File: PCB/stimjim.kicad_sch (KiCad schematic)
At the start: 21 parts, among them J1 Conn_02x08_Odd_Even, J10 USB4105-GF-A, J11 BM03B-SRSS-TB, J4 10129383-910002ALF, U151 AP2112K-3.3

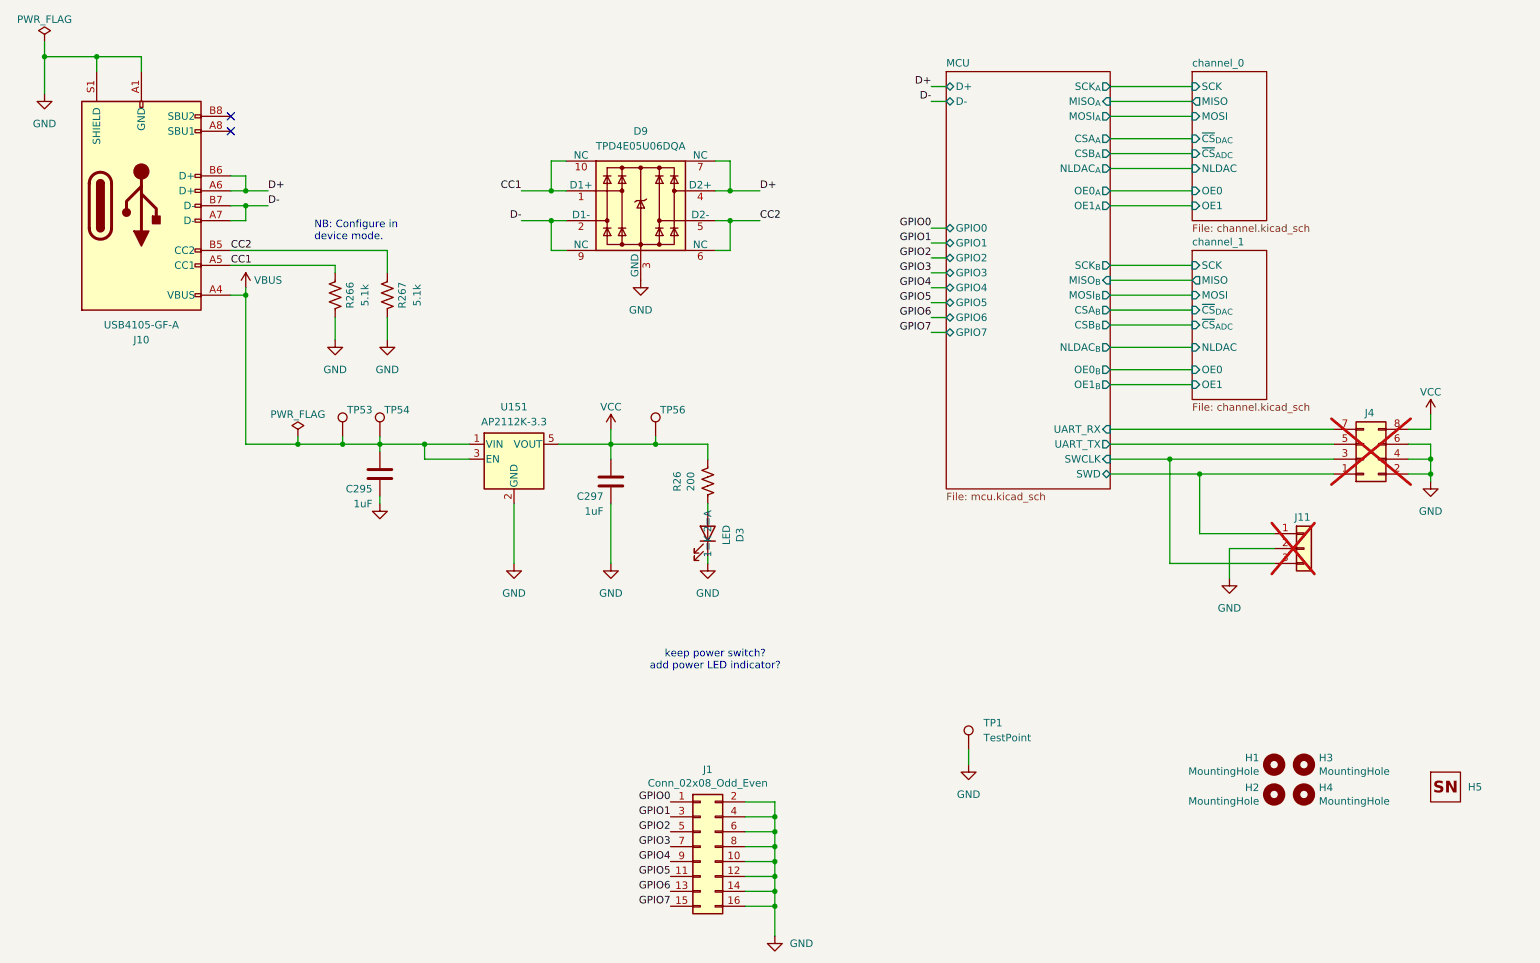
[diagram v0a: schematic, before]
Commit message: Stimjim Rev. B candidate
- Sent to fab
- Lots of manufacturability changes
- BOM consolidation
- Repo layout changed a bit to remove redundant information. e.g.
  datasheet links are embedded in schematic. BOM information embedded in
  schematic. etc
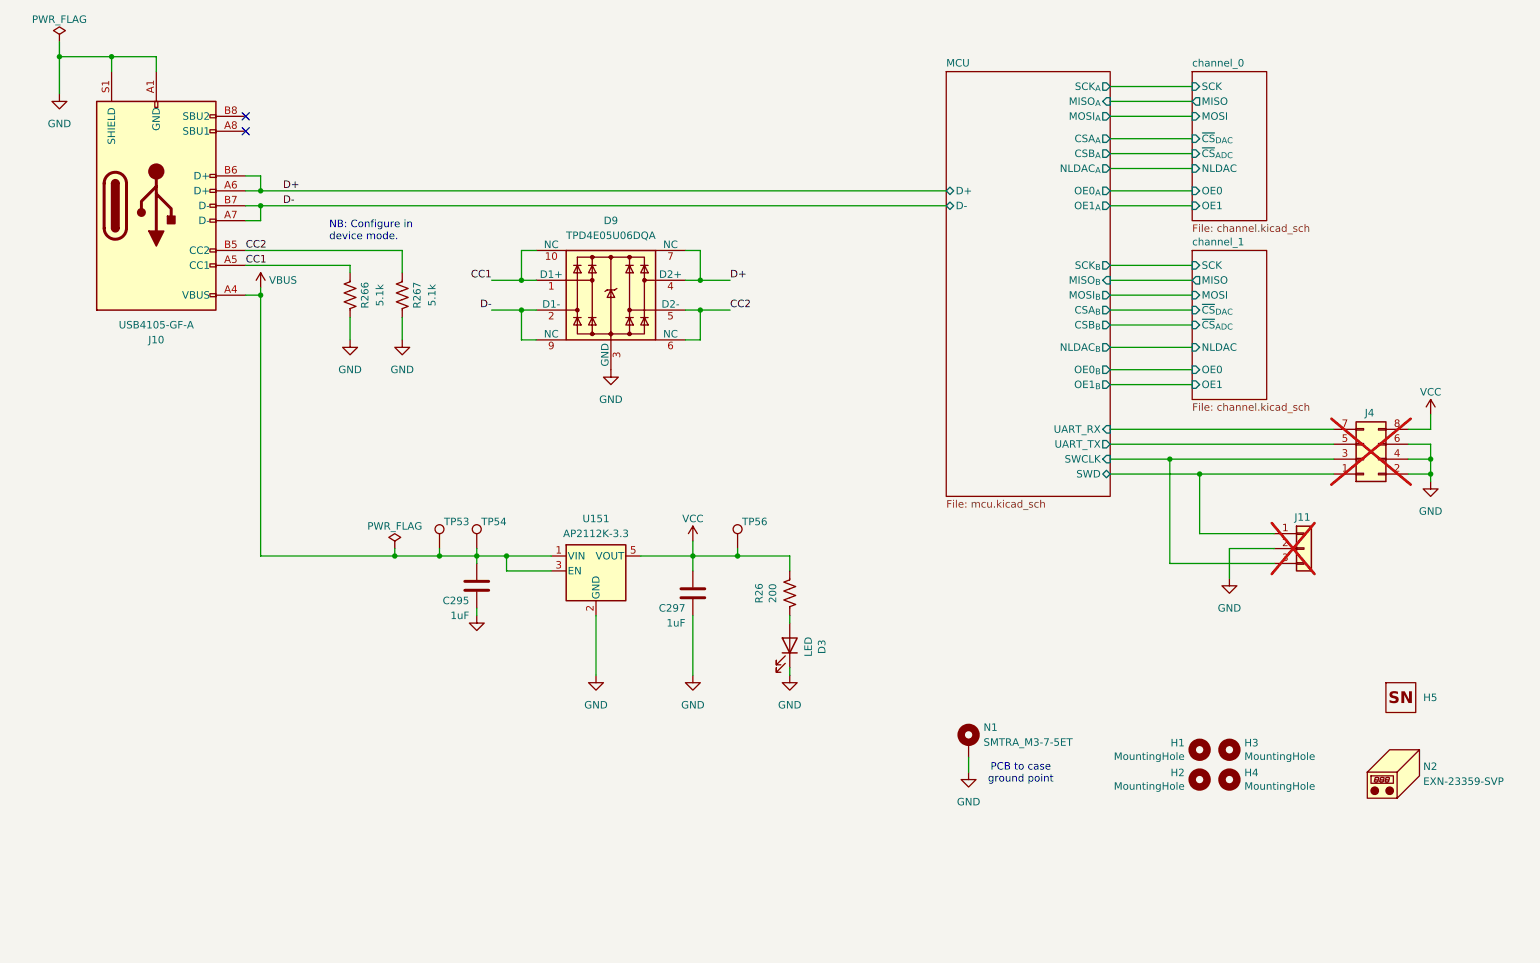
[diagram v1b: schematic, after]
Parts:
- removed J1: Conn_02x08_Odd_Even, Connector_IDC:IDC-Header_2x08_P2.54mm_Horizontal, symbol Connector_Generic:Conn_02x08_Odd_Even
- added N2: EXN-23359-SVP, symbol Mechanical:Housing
- C295, C297: Voltage 16V -> 25V
- D3: MPN (none) -> SSF-LXH100GD-01; now in the parts list
- D9: MPN (none) -> TPD4E05U06DQA
- J10: MPN (none) -> USB4105-GF-A
- J11: MPN (none) -> BM03B-SRSS-TB
- J4: MPN (none) -> 10129383-910002ALF
- N1: renamed from TP1; value TestPoint -> SMTRA_M3-7-5ET; symbol Connector:TestPoint -> Mechanical:MountingHole_Pad; MPN (none) -> SMTRA_M3-7-5ET
- R266, R267: Tolerance (none) -> 1%
- U151: MPN (none) -> AP2112K-3.3
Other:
- sheet MCU ports: added none; removed GPIO0, GPIO1, GPIO2, GPIO3, GPIO4, GPIO5, GPIO6, GPIO7
- note added: "PCB to case ground point"
- note removed: "keep power switch? add power LED indicator?"
- company: Nate Cermak and Jon Newman -> (none)
- moved on the sheet: C295, C297, D3, D9, H1, H2, H3, H4, H5, J10, R26, R266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

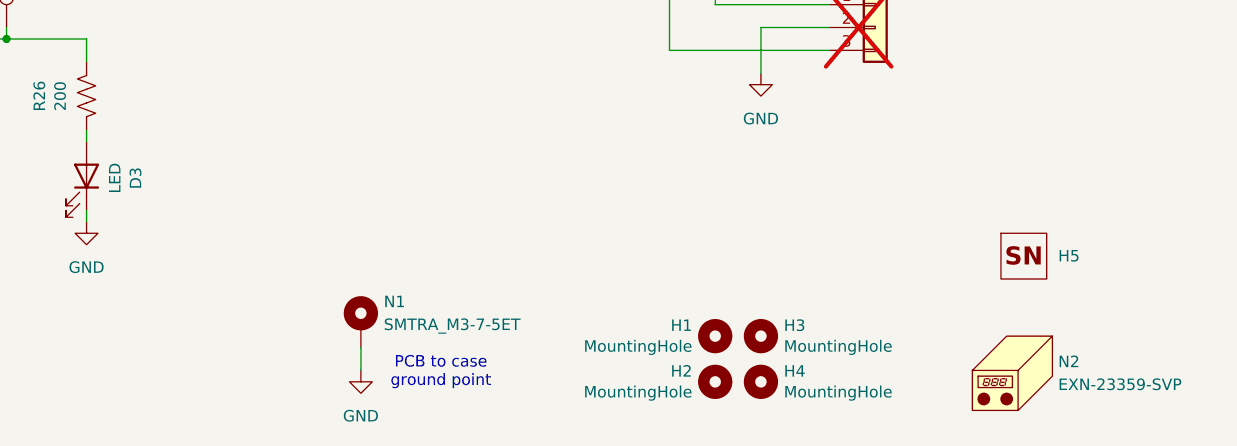
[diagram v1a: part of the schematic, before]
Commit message: Rev C First Draft
- Fix and move LED footprints
- Move bar code sticker
- Add op-amp unity voltage follower to ADC input
- Remove screw terminals
- Made panel screw holes bigger both panels (3.2mm -> 3.7mm) for 3.4mm
  screws
- Create cutout for mounting rail on panels
- Delete the file with both back and front panels
- Update all footprints (except rp2354b so that its thermal vias pass DRC)
- Add component class and custom rule for USB-C footprint
- Indicate M3 screw in schematic + Add to BOM
- Improve adherence to ADC/DAC datasheets:
  - Move high speed signals out from under ADC (put MISO in +5V layer under ADC)
  - Add 10uF decoupling caps to ADC/DAC
- Change enclosure part number to black enclosure
- Add some more GND vias to isolated GND planes
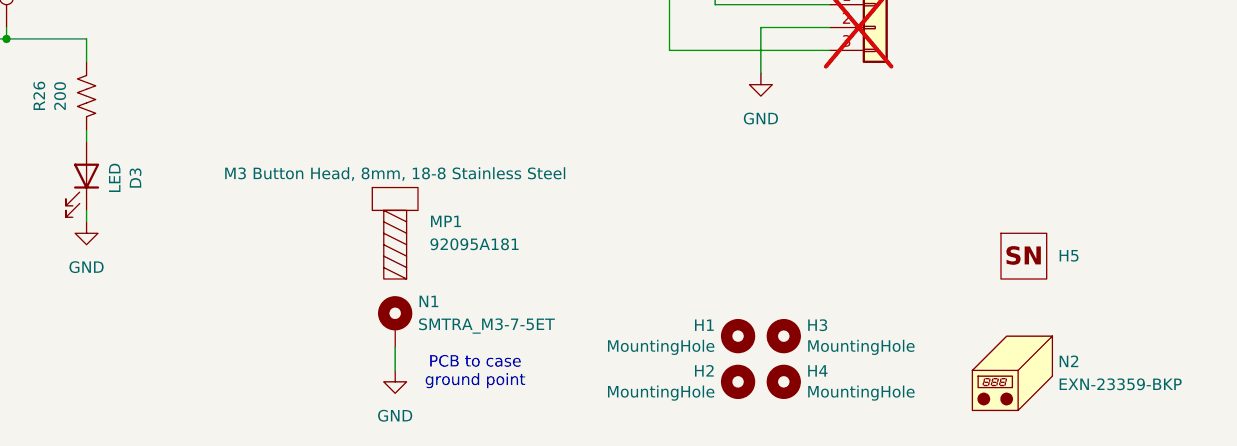
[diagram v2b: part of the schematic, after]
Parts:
- added MP1: 92095A181, symbol open-ephys:Screw
- D3: footprint microstim:LED_D5.0mm_Horizontal_O1.27mm_Z3.0mm_pinSwapped -> open-ephys:LUMEX_SSF-LHXH100GD-01
- J10: Component Class (none) -> USB
- N2: value EXN-23359-SVP -> EXN-23359-BKP
- R26: now in the parts list
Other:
- moved on the sheet: H1, H2, H3, H4, N1

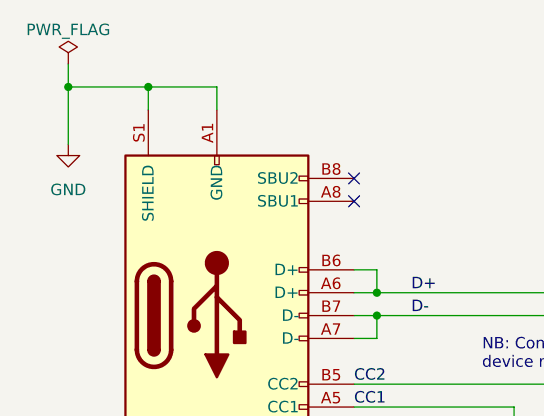
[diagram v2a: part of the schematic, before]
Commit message: Replace amplifiers
- INA826 -> AD8421
- AMP03 -> LT1995 w/ op-amp in feedback circuit
- Also:
  - update to kicad v10
  - utilize multi-channel layout feature
  - update calculations on schematic
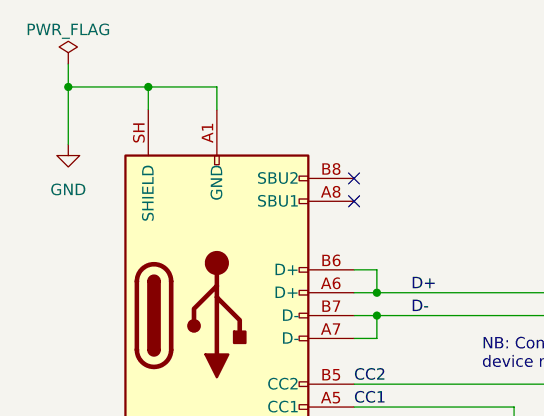
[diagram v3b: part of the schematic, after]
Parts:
- H5: value ~ -> (none)
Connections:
- net GND: now also J10.SH (SHIELD); no longer J10.S1 (SHIELD)
